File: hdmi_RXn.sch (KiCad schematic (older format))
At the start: 40 parts

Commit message: Always have a prefix 1.
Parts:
- renumbered C$RXn$01 to C$RXn$11, C$RXn$10 to C$RXn$110, C$RXn$11 to C$RXn$111, C$RXn$12 to C$RXn$112, C$RXn$13 to C$RXn$113, C$RXn$14 to C$RXn$114, C$RXn$15 to C$RXn$115, C$RXn$02 to C$RXn$12, C$RXn$03 to C$RXn$13, C$RXn$04 to C$RXn$14, C$RXn$05 to C$RXn$15, C$RXn$06 to C$RXn$16, C$RXn$07 to C$RXn$17, C$RXn$08 to C$RXn$18, C$RXn$09 to C$RXn$19, D$RXn$01 to D$RXn$11, D$RXn$02 to D$RXn$12, D$RXn$03 to D$RXn$13, FB$RXn$01 to FB$RXn$11, FB$RXn$02 to FB$RXn$12, FB$RXn$03 to FB$RXn$13, FB$RXn$04 to FB$RXn$14, J$RXn$1 to J$RXn$11, P$RXn$01 to P$RXn$11, Q$RXn$01 to Q$RXn$11, Q$RXn$02 to Q$RXn$12, Q$RXn$03 to Q$RXn$13, R$RXn$01 to R$RXn$11, R$RXn$10 to R$RXn$110, R$RXn$11 to R$RXn$111, R$RXn$12 to R$RXn$112, R$RXn$02 to R$RXn$12, R$RXn$03 to R$RXn$13, R$RXn$04 to R$RXn$14, R$RXn$05 to R$RXn$15, R$RXn$06 to R$RXn$16, R$RXn$07 to R$RXn$17, R$RXn$08 to R$RXn$18, R$RXn$09 to R$RXn$19, U$RXn$1 to U$RXn$11
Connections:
- net labels added: HDMIP_$RXn$1_D1+, HDMIP_$RXn$1_D1-, HDMIP_$RXn$1_D2+, HDMIP_$RXn$1_D2-, HDMIP_$RXn$1_D3+, HDMIP_$RXn$1_D3-, HDMIP_$RXn$1_D4+, HDMIP_$RXn$1_D4-, HDMIP_$RXn$1_HPD, HDMIP_$RXn$1_SCL, HDMIP_$RXn$1_SDA, HDMI_$RXn$1_CEC, HDMI_$RXn$1_D1+, HDMI_$RXn$1_D1-, HDMI_$RXn$1_D2+, HDMI_$RXn$1_D2-, HDMI_$RXn$1_D3+, HDMI_$RXn$1_D3-, HDMI_$RXn$1_D4+, HDMI_$RXn$1_D4-, HDMI_$RXn$1_HPA, HDMI_$RXn$1_IO0, HDMI_$RXn$1_IO1, HDMI_$RXn$1_PEEN, HDMI_$RXn$1_SCL, HDMI_$RXn$1_SDA, HDMI_$RXn$1_TMDS[4..1], HDMI_$RXn$1_TXEN, VCC5V0_$RXn$1
- net labels removed: HDMIP_$RXn$_D1+, HDMIP_$RXn$_D1-, HDMIP_$RXn$_D2+, HDMIP_$RXn$_D2-, HDMIP_$RXn$_D3+, HDMIP_$RXn$_D3-, HDMIP_$RXn$_D4+, HDMIP_$RXn$_D4-, HDMIP_$RXn$_HPD, HDMIP_$RXn$_SCL, HDMIP_$RXn$_SDA, HDMI_$RXn$_CEC, HDMI_$RXn$_D1+, HDMI_$RXn$_D1-, HDMI_$RXn$_D2+, HDMI_$RXn$_D2-, HDMI_$RXn$_D3+, HDMI_$RXn$_D3-, HDMI_$RXn$_D4+, HDMI_$RXn$_D4-, HDMI_$RXn$_HPA, HDMI_$RXn$_IO0, HDMI_$RXn$_IO1, HDMI_$RXn$_PEEN, HDMI_$RXn$_SCL, HDMI_$RXn$_SDA, HDMI_$RXn$_TMDS[4..1], HDMI_$RXn$_TXEN, VCC5V0_$RXn$

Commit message: Change annotation numbering scheme.
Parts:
- renumbered C$RXn$11 to C$RXn$101, C$RXn$12 to C$RXn$102, C$RXn$13 to C$RXn$103, C$RXn$14 to C$RXn$104, C$RXn$15 to C$RXn$105, C$RXn$16 to C$RXn$106, C$RXn$17 to C$RXn$107, C$RXn$18 to C$RXn$108, C$RXn$19 to C$RXn$109, D$RXn$11 to D$RXn$101, D$RXn$12 to D$RXn$102, D$RXn$13 to D$RXn$103, FB$RXn$11 to FB$RXn$101, FB$RXn$12 to FB$RXn$102, FB$RXn$13 to FB$RXn$103, FB$RXn$14 to FB$RXn$104, P$RXn$11 to P$RXn$1, Q$RXn$11 to Q$RXn$101, Q$RXn$12 to Q$RXn$102, Q$RXn$13 to Q$RXn$103, R$RXn$11 to R$RXn$101, R$RXn$12 to R$RXn$102, R$RXn$13 to R$RXn$103, R$RXn$14 to R$RXn$104, R$RXn$15 to R$RXn$105, R$RXn$16 to R$RXn$106, R$RXn$17 to R$RXn$107, R$RXn$18 to R$RXn$108, R$RXn$19 to R$RXn$109

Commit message: Small fixes to major component numbers.
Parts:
- renumbered J$RXn$11 to J$RXn$1, U$RXn$11 to U$RXn$1
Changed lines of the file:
@@
 $EndDescr
 $Comp
-L AD8195 U$RXn$11
+L AD8195 U$RXn$1
 U 1 1 57C07766
 P 8050 2850
-F 0 "U$RXn$11" H 8700 1700 60  0000 C CNN
+F 0 "U$RXn$1" H 8700 1700 60  0000 C CNN
 F 1 "AD8195" H 8050 2950 60  0000 C CNN
 F 2 "Housings_DFN_QFN:QFN-40-1EP_6x6mm_Pitch0.5mm" H 8000 2850 60  0001 C CNN
@@
 $EndComp
 $Comp
-L HDMI J$RXn$11
+L HDMI J$RXn$1
 U 1 1 57C077DA
 P 4750 3000
-F 0 "J$RXn$11" H 4600 4050 60  0000 C CNN
+F 0 "J$RXn$1" H 4600 4050 60  0000 C CNN
 F 1 "HDMI" V 4900 3000 60  0000 C CNN
 F 2 "" H 4700 3000 60  0001 C CNN

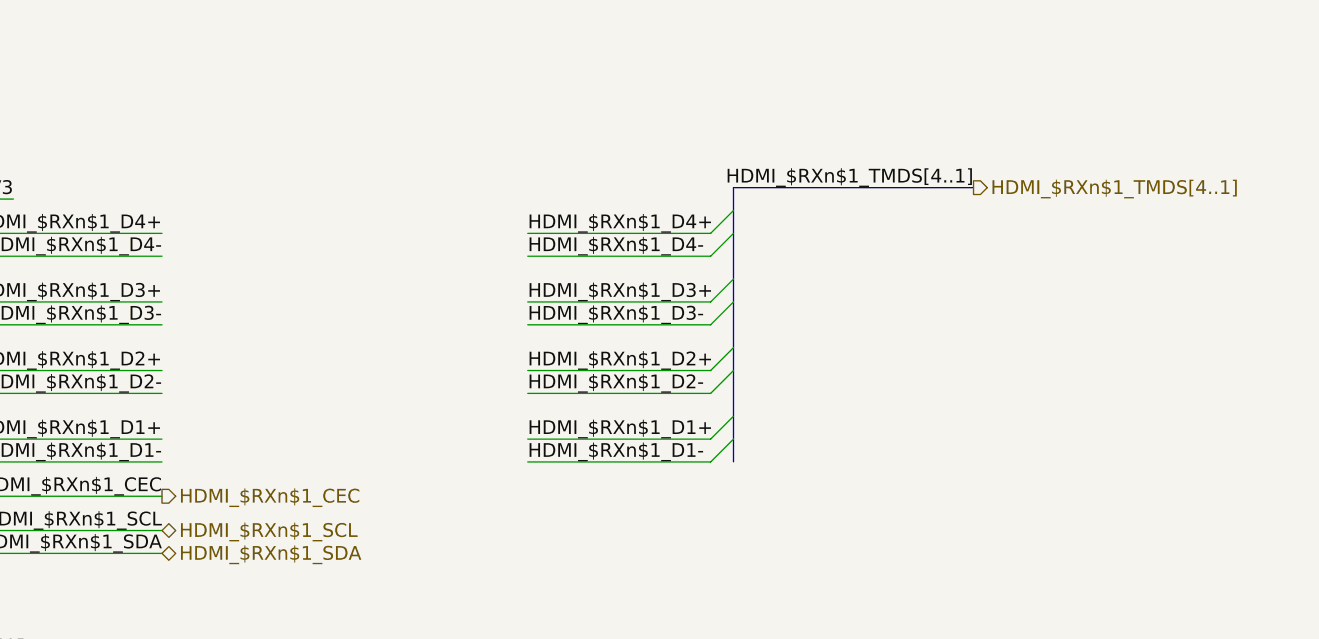
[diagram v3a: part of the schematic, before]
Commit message: Getting rid of busses.
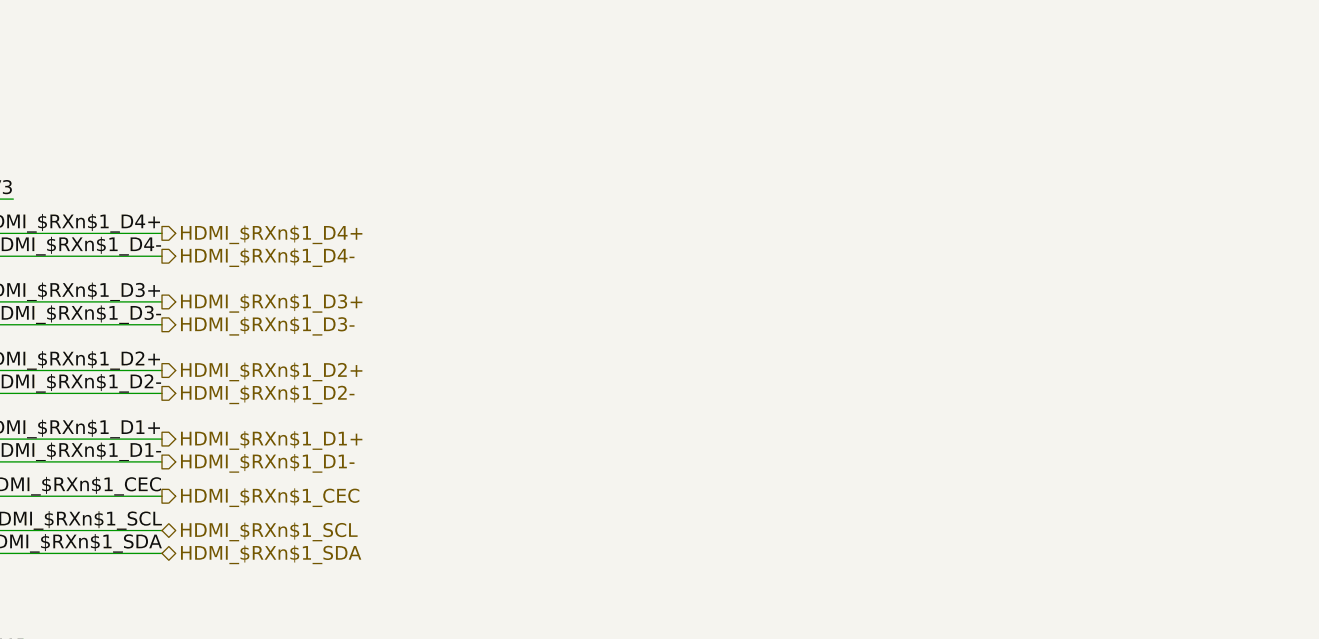
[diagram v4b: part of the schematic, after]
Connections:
- net labels removed: HDMI_$RXn$1_TMDS[4..1]
- wire segments 184 -> 176
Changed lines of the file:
@@
 LIBS:hdmi2usb
 LIBS:HDMI2USB-cache
-LIBS:hdmi_RXn-cache
 EELAYER 25 0
 EELAYER END
@@
 Text HLabel 1500 6600 0    60   Input ~ 0
 HDMI_$RXn$1_HPA
-Text Label 11700 3000 0    60   ~ 0
-HDMI_$RXn$1_D1+
-Text Label 11700 3100 0    60   ~ 0
-HDMI_$RXn$1_D1-
-Text Label 11700 2800 0    60   ~ 0
-HDMI_$RXn$1_D2-
-Text Label 11700 2700 0    60   ~ 0
-HDMI_$RXn$1_D2+
-Text Label 11700 2500 0    60   ~ 0
-HDMI_$RXn$1_D3-
-Text Label 11700 2400 0    60   ~ 0
-HDMI_$RXn$1_D3+
-Text Label 11700 2200 0    60   ~ 0
-HDMI_$RXn$1_D4-
-Text Label 11700 2100 0    60   ~ 0
-HDMI_$RXn$1_D4+
-Entry Wire Line
-	12500 2100 12600 2000
-Entry Wire Line
-	12500 2200 12600 2100
-Entry Wire Line
-	12500 2400 12600 2300
-Entry Wire Line
-	12500 2500 12600 2400
-Entry Wire Line
-	12500 2700 12600 2600
-Entry Wire Line
-	12500 2800 12600 2700
-Entry Wire Line
-	12500 3000 12600 2900
-Entry Wire Line
-	12500 3100 12600 3000
-Text HLabel 13650 1900 2    60   Output ~ 0
-HDMI_$RXn$1_TMDS[4..1]
-Text Label 13650 1900 2    60   ~ 0
-HDMI_$RXn$1_TMDS[4..1]
 Wire Wire Line
 	5300 2100 7150 2100
@@
 Wire Wire Line
 	6950 1750 6950 1650
-Wire Wire Line
-	11700 2100 12500 2100
-Wire Wire Line
-	11700 2200 12500 2200
-Wire Wire Line
-	11700 2400 12500 2400
-Wire Wire Line
-	11700 2500 12500 2500
-Wire Wire Line
-	11700 2700 12500 2700
-Wire Wire Line
-	11700 2800 12500 2800
-Wire Wire Line
-	11700 3000 12500 3000
-Wire Wire Line
-	11700 3100 12500 3100
-Wire Bus Line
-	12600 1900 12600 3100
-Wire Bus Line
-	12600 1900 13650 1900
 Wire Wire Line
 	2050 1400 2050 1450
@@
 Wire Wire Line
 	6290 7100 6250 7100
+Text HLabel 10100 2100 2    60   Output ~ 0
+HDMI_$RXn$1_D4+
+Text HLabel 10100 2200 2    60   Output ~ 0
+HDMI_$RXn$1_D4-
+Text HLabel 10100 2400 2    60   Output ~ 0
+HDMI_$RXn$1_D3+
+Text HLabel 10100 2500 2    60   Output ~ 0
+HDMI_$RXn$1_D3-
+Text HLabel 10100 2700 2    60   Output ~ 0
+HDMI_$RXn$1_D2+
+Text HLabel 10100 2800 2    60   Output ~ 0
+HDMI_$RXn$1_D2-
+Text HLabel 10100 3000 2    60   Output ~ 0
+HDMI_$RXn$1_D1+
+Text HLabel 10100 3100 2    60   Output ~ 0
+HDMI_$RXn$1_D1-
 $EndSCHEMATC

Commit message: Add VCC5V0 global label for 5V rail for hdmi rx buffer
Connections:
- wire segments 176 -> 227
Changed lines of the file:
@@
 LIBS:hdmi2usb
 LIBS:HDMI2USB-cache
+LIBS:hdmi_RXn-cache
 EELAYER 25 0
 EELAYER END
@@
 Text Label 6200 1150 2    60   ~ 0
 VCC5V0_$RXn$1
-Text Label 6200 950  2    60   ~ 0
-VCC5V0
 $Comp
 L FILTER FB$RXn$104
@@
 	6150 3200 6150 3100
 Wire Wire Line
-	5800 3100 7150 3100
+	5800 3100 6150 3100
+Wire Wire Line
+	6150 3100 7150 3100
 Wire Wire Line
 	5300 3300 6250 3300
@@
 	5300 2800 5550 2800
 Wire Wire Line
-	7850 4150 7850 4300
-Wire Wire Line
-	9050 4250 7600 4250
+	7850 4150 7850 4250
+Wire Wire Line
+	7850 4250 7850 4300
+Wire Wire Line
+	9050 4250 8300 4250
+Wire Wire Line
+	8300 4250 8150 4250
+Wire Wire Line
+	8150 4250 8000 4250
+Wire Wire Line
+	8000 4250 7850 4250
+Wire Wire Line
+	7850 4250 7600 4250
 Wire Wire Line
 	8300 4250 8300 4150
@@
 Connection ~ 8300 4250
 Wire Wire Line
-	6750 950  6750 1350
-Wire Wire Line
-	6750 1150 7550 1150
+	6750 950  6750 1150
+Wire Wire Line
+	6750 1150 6750 1350
+Wire Wire Line
+	6750 1150 6950 1150
+Wire Wire Line
+	6950 1150 7100 1150
+Wire Wire Line
+	7100 1150 7550 1150
 Wire Wire Line
 	7550 1150 7550 1400
@@
 	7750 1250 7750 1400
 Wire Wire Line
-	7750 1250 8350 1250
+	7750 1250 7850 1250
+Wire Wire Line
+	7850 1250 7950 1250
+Wire Wire Line
+	7950 1250 8050 1250
+Wire Wire Line
+	8050 1250 8150 1250
+Wire Wire Line
+	8150 1250 8250 1250
+Wire Wire Line
+	8250 1250 8350 1250
 Wire Wire Line
 	8350 1250 8350 1400
@@
 Connection ~ 7950 1250
 Wire Wire Line
-	8050 1050 8050 1400
+	8050 1050 8050 1250
+Wire Wire Line
+	8050 1250 8050 1400
 Connection ~ 8050 1250
 Wire Wire Line
@@
 	10350 5900 10350 6150
 Wire Wire Line
-	10200 5300 10200 5600
+	10200 5300 10200 5400
+Wire Wire Line
+	10200 5400 10200 5600
 Wire Wire Line
 	10200 5400 10350 5400
@@
 Connection ~ 10200 5400
 Wire Wire Line
-	10200 4150 10200 4450
+	10200 4150 10200 4250
+Wire Wire Line
+	10200 4250 10200 4450
 Wire Wire Line
 	10200 4250 10350 4250
@@
 	700  1850 1300 1850
 Wire Wire Line
-	2000 1850 3050 1850
+	2000 1850 2050 1850
+Wire Wire Line
+	2050 1850 2350 1850
+Wire Wire Line
+	2350 1850 2650 1850
+Wire Wire Line
+	2650 1850 3050 1850
 Wire Wire Line
 	2650 1850 2650 2000
@@
 Connection ~ 2050 1850
 Wire Wire Line
-	2000 2650 3050 2650
+	2000 2650 2050 2650
+Wire Wire Line
+	2050 2650 2350 2650
+Wire Wire Line
+	2350 2650 2650 2650
+Wire Wire Line
+	2650 2650 3050 2650
 Wire Wire Line
 	2650 2650 2650 2800
@@
 Connection ~ 2050 2650
 Wire Wire Line
-	2000 950  4000 950
+	2000 950  2050 950
+Wire Wire Line
+	2050 950  2350 950
+Wire Wire Line
+	2350 950  2650 950
+Wire Wire Line
+	2650 950  2950 950
+Wire Wire Line
+	2950 950  3250 950
+Wire Wire Line
+	3250 950  3550 950
+Wire Wire Line
+	3550 950  4000 950
 Wire Wire Line
 	3550 950  3550 1100
@@
 Connection ~ 2050 950
 Wire Wire Line
-	700  1450 3550 1450
+	700  1450 2050 1450
+Wire Wire Line
+	2050 1450 2350 1450
+Wire Wire Line
+	2350 1450 2650 1450
+Wire Wire Line
+	2650 1450 2950 1450
+Wire Wire Line
+	2950 1450 3250 1450
+Wire Wire Line
+	3250 1450 3550 1450
 Connection ~ 3250 1450
 Connection ~ 2950 1450
@@
 Connection ~ 2050 1450
 Wire Wire Line
-	700  2350 2650 2350
+	700  2350 2050 2350
+Wire Wire Line
+	2050 2350 2350 2350
+Wire Wire Line
+	2350 2350 2650 2350
 Connection ~ 2350 2350
 Wire Wire Line
-	700  3150 2650 3150
+	700  3150 2050 3150
+Wire Wire Line
+	2050 3150 2350 3150
+Wire Wire Line
+	2350 3150 2650 3150
 Connection ~ 2050 3150
 Connection ~ 2050 2350
@@
 	6950 3650 6950 4900
 Wire Wire Line
-	6950 4900 6050 4900
+	6950 4900 6600 4900
+Wire Wire Line
+	6600 4900 6050 4900
 Wire Wire Line
 	7150 3750 7050 3750
@@
 	7050 3750 7050 5000
 Wire Wire Line
-	7050 5000 6050 5000
+	7050 5000 6300 5000
+Wire Wire Line
+	6300 5000 6050 5000
 Wire Wire Line
 	6600 4900 6600 5150
 Connection ~ 6600 4900
 Wire Wire Line
-	6300 4850 6300 5150
+	6300 4850 6300 5000
+Wire Wire Line
+	6300 5000 6300 5150
 Connection ~ 6300 5000
 Wire Wire Line
@@
 	6300 5550 6000 5550
 Wire Wire Line
-	5750 7000 5300 7000
-Wire Wire Line
-	5750 7100 5300 7100
+	5750 7000 5690 7000
+Wire Wire Line
+	5690 7000 5300 7000
+Wire Wire Line
+	5750 7100 5650 7100
+Wire Wire Line
+	5650 7100 5300 7100
 Wire Wire Line
 	4950 6700 5750 6700
@@
 	4950 6800 5750 6800
 Wire Wire Line
-	1500 6600 2300 6600
+	1500 6600 2100 6600
+Wire Wire Line
+	2100 6600 2300 6600
 Wire Wire Line
 	2100 6600 2100 6750
 Connection ~ 2100 6600
 Wire Wire Line
-	1500 7150 3100 7150
+	1500 7150 2100 7150
+Wire Wire Line
+	2100 7150 2500 7150
+Wire Wire Line
+	2500 7150 3100 7150
 Wire Wire Line
 	2500 6400 2500 6300
 Wire Wire Line
-	2500 6300 2900 6300
+	2500 6300 2600 6300
+Wire Wire Line
+	2600 6300 2900 6300
 Wire Wire Line
 	2600 6150 2600 6300
@@
 	3100 4800 3100 5600
 Wire Wire Line
-	3100 5900 3100 6100
+	3100 5900 3100 6050
+Wire Wire Line
+	3100 6050 3100 6100
 Wire Wire Line
 	3100 6050 3950 6050
@@
 	4150 4800 4150 4850
 Wire Wire Line
-	1900 4800 4150 4800
+	1900 4800 2600 4800
+Wire Wire Line
+	2600 4800 3100 4800
+Wire Wire Line
+	3100 4800 4150 4800
 Connection ~ 3100 4800
 Connection ~ 2600 4800
@@
 	6750 1650 6750 1750
 Wire Wire Line
-	6750 1750 6950 1750
+	6750 1750 6850 1750
+Wire Wire Line
+	6850 1750 6950 1750
 Wire Wire Line
 	6950 1750 6950 1650
@@
 Text HLabel 10100 3100 2    60   Output ~ 0
 HDMI_$RXn$1_D1-
+Text GLabel 6200 950  0    60   Input ~ 0
+VCC5V0
 $EndSCHEMATC
